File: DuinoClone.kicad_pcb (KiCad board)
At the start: 2 copper layers, 41.4 x 27.7 mm, 17 parts, among them J1 Digital pins, J2 Serial, J3 ICSP, J4 I2C, U1 DS1337S+, U2 24LC1025, U3 24LC1025, U4 ATMEGA328P-AU, Y1 Crystal 32MHz, Y2 Crystal 16MHz

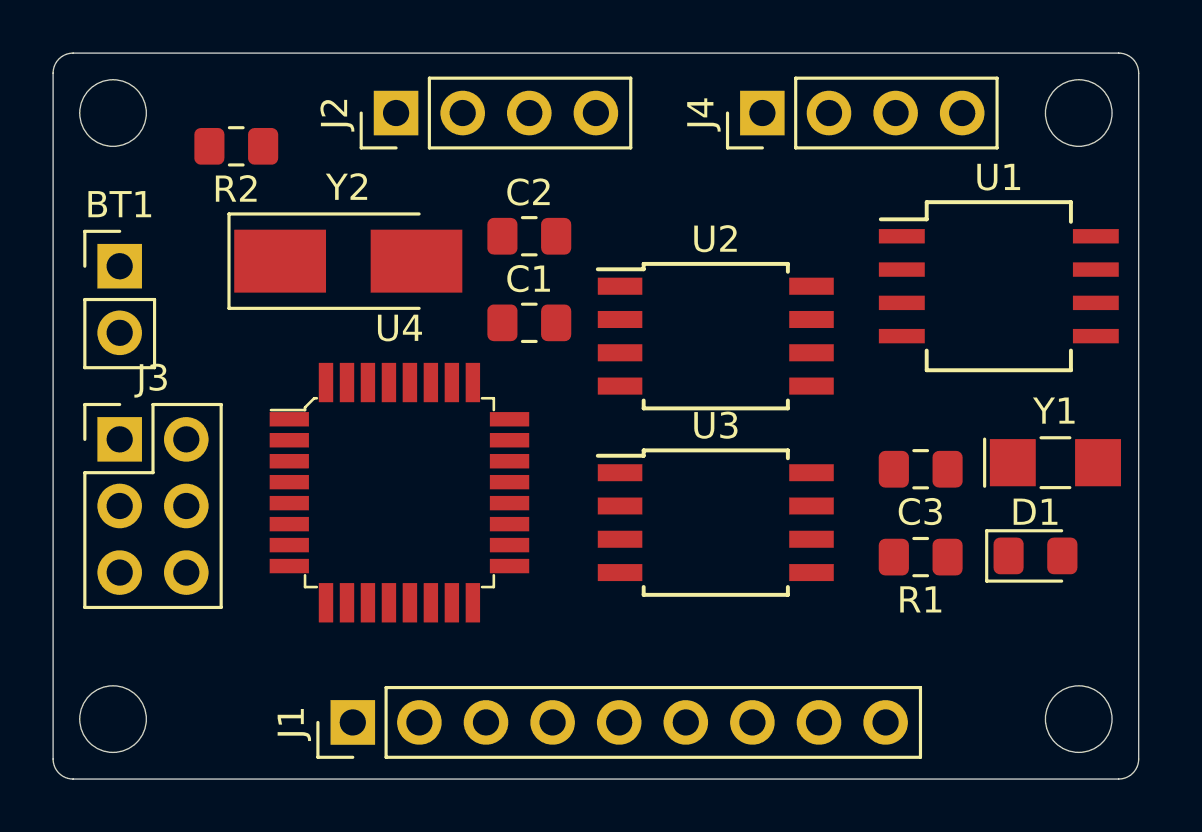
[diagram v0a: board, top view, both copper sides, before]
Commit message: Created copper filled area for 2-layer board
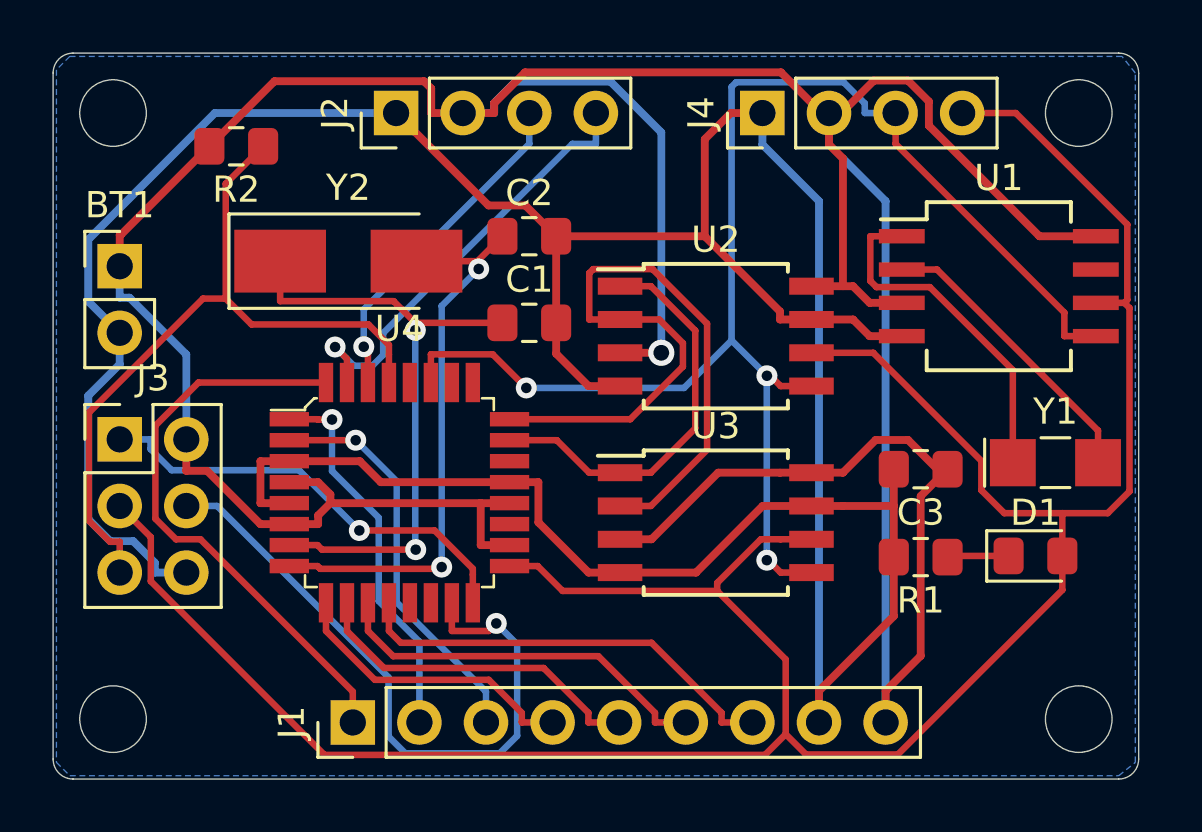
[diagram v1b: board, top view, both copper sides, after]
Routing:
- net /Vcc: track 0.00 -> 153.7 mm, vias 0 -> 1
- net GNDPWR: track 0.00 -> 132.5 mm
- net /SCK: track 0.00 -> 101.6 mm
- net /SDA: track 0.00 -> 55.6 mm, vias 0 -> 3
- net /RESET: track 0.00 -> 28.6 mm
- net /ADDS2: track 0.00 -> 28.5 mm
- net /MOSI: track 0.00 -> 25.6 mm, vias 0 -> 1
- net Net-(C1-Pad1): track 0.00 -> 23.9 mm, vias 0 -> 2
- net /D2: track 0.00 -> 22.2 mm
- net Net-(C2-Pad1): track 0.00 -> 21.9 mm, vias 0 -> 2
- net /MISO: track 0.00 -> 17.0 mm, vias 0 -> 1
- net /TX: track 0.00 -> 17.0 mm, vias 0 -> 1
- net /D8: track 0.00 -> 16.6 mm
- net /ADDS1: track 0.00 -> 15.6 mm
- net /D4: track 0.00 -> 15.4 mm, vias 0 -> 1
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- added copper zone on B.Cu, net GNDPWR

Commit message: Completed Silk Screen for front copper layer
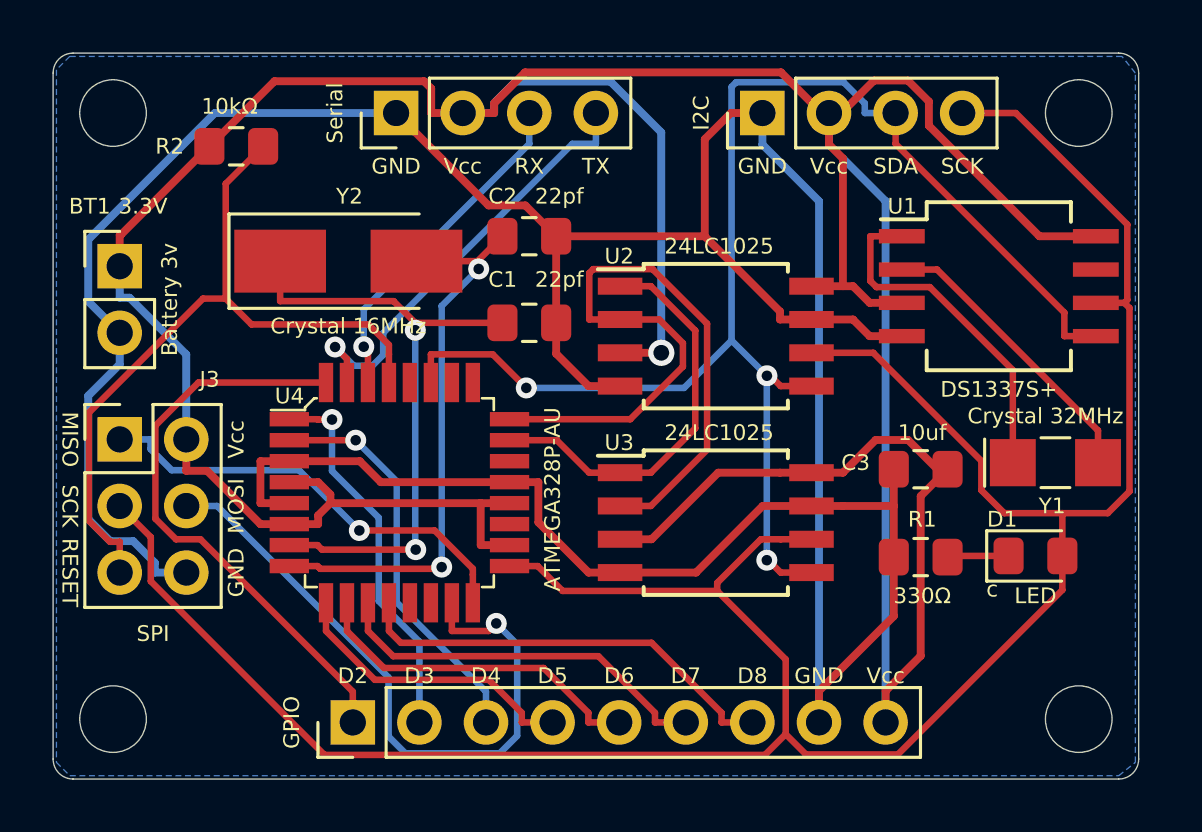
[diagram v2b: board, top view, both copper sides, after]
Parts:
- J3: value ICSP -> SPI
- R1: value 330ohm -> 330Ω
- R2: value 10kohm -> 10kΩ
- renumbered J1 to GPIO, J4 to I2C, J2 to Serial
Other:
- board text added: "3.3V"
- board text added: "D2"
- board text added: "D3"
- board text added: "D4"
- board text added: "D5"
- board text added: "D6"
- board text added: "D7"
- board text added: "D8"
- board text added: "GND"
- board text added: "MISO"
- board text added: "MOSI"
- board text added: "RESET"
- board text added: "RX"
- board text added: "SCK"
- board text added: "SDA"
- board text added: "TX"
- board text added: "Vcc"
- board text added: "c"

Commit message: Completed Silkscreen work
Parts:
- added G***: LOGO, KiCad Graphics:3HitComboPCBLogo, B.Cu at (112.1, 92.7)
- added REF**: OSHW-Logo2_9.8x8mm_SilkScreen, Symbol:OSHW-Logo2_9.8x8mm_SilkScreen, B.Cu at (101.3, 93.6)
- added REF**: KiCad-Logo2_6mm_SilkScreen, Symbol:KiCad-Logo2_6mm_SilkScreen, B.Cu at (94.1, 98.6)
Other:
- board text added: "Arduino clone featuring: * 2Mbit EEPROM * Clock & Calendar * I2C, SPI, GPIO Connections Designed by Anthony Hollis http://iRootAndCode.com"
